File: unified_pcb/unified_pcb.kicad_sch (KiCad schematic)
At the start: 96 parts, among them J1 Conn_01x02_Socket, J2 USB_C_Receptacle, J3 Conn_01x02_Socket, J4 Conn_01x03_Pin, Q1 Q_Photo_NPN, Q2 Q_Photo_NPN, Q3 Q_Photo_NPN, SW1 SW_Push, SW2 SW_Push, U1 BQ27427YZFR, U10 3.3V LDO, U11 LMD4030T261-OA1, U12 LY4176D, U13 MMC5603NJ, U14 BMI270, U2 USBLC6-2P6, U3 3.3V LDO, U4 RP2350_60QFN, U7 QSPI Flash, U8 TPGLF72101CSP4, Y1 12MHz

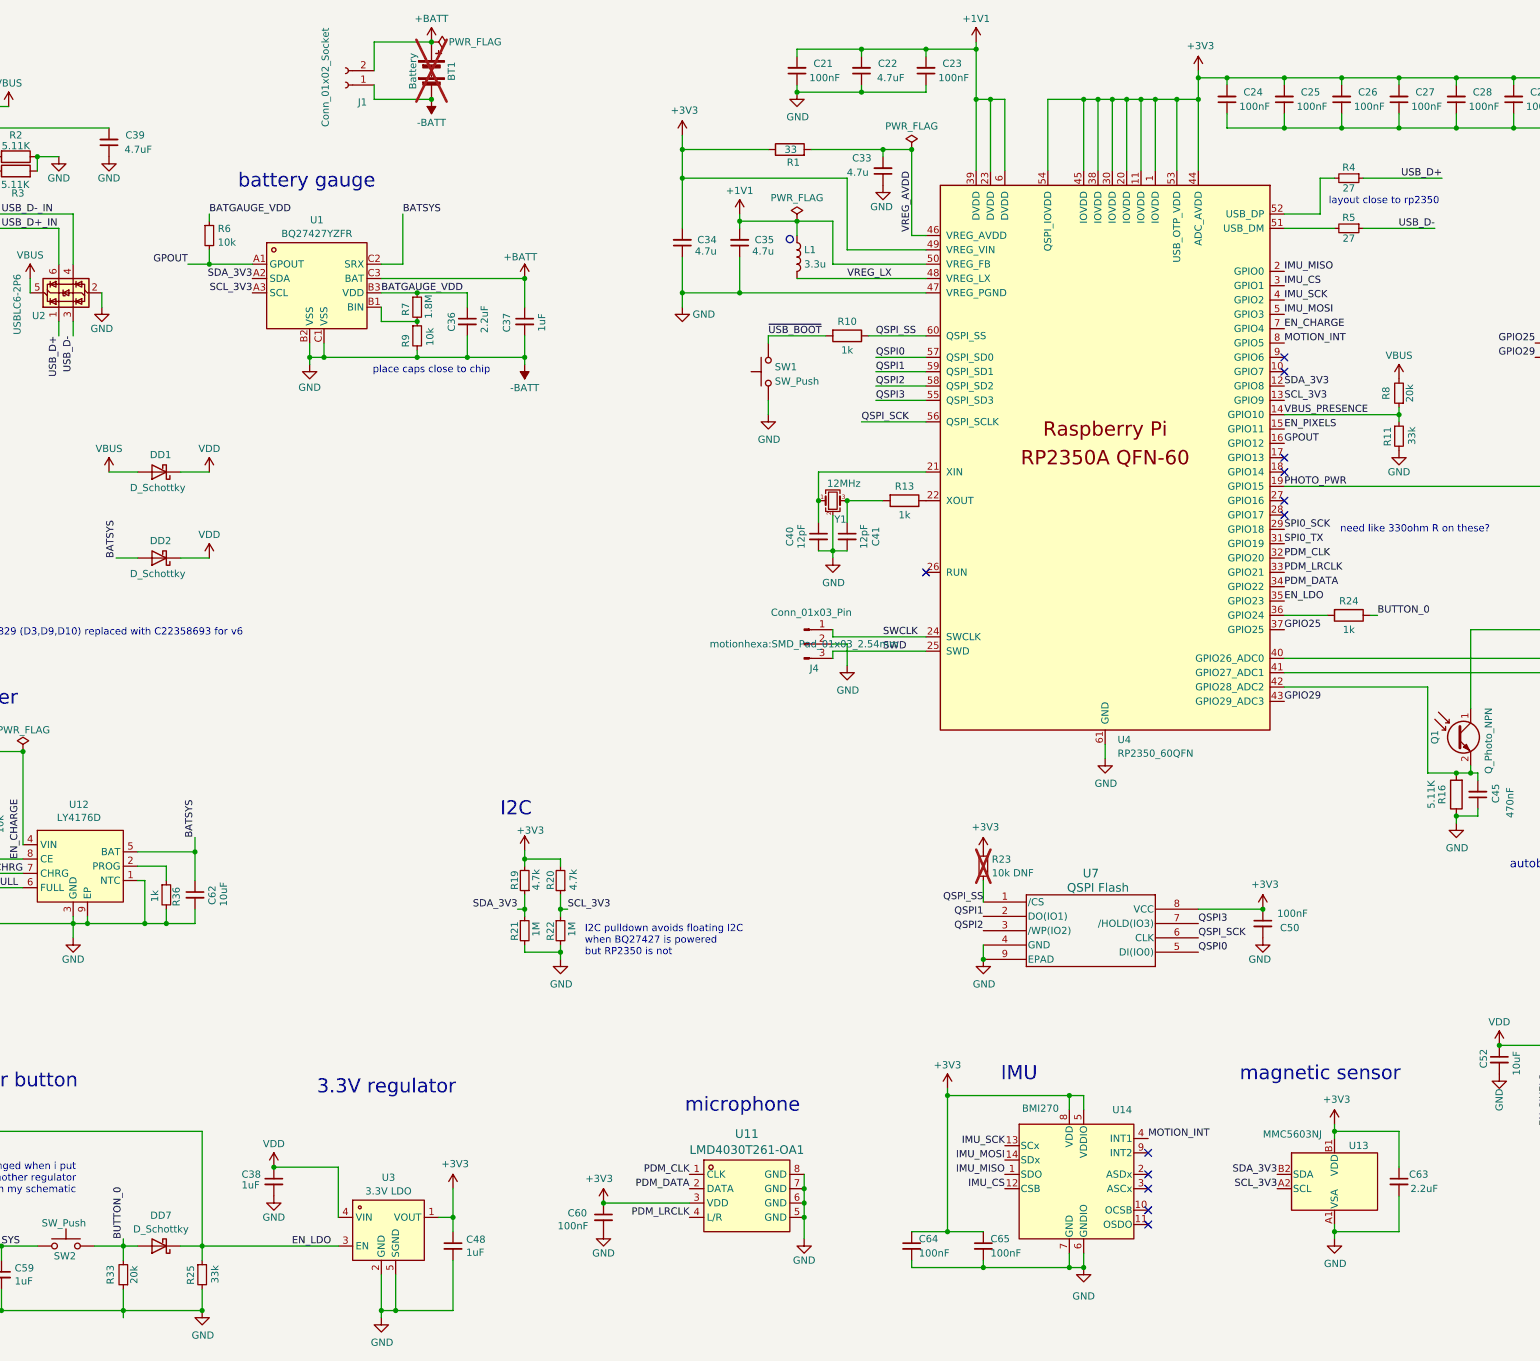
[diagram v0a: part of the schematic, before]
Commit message: ticking with dual ldo because moving to mosfets is unnecessary churn; lay out for magnetic sensor; layout cleanup
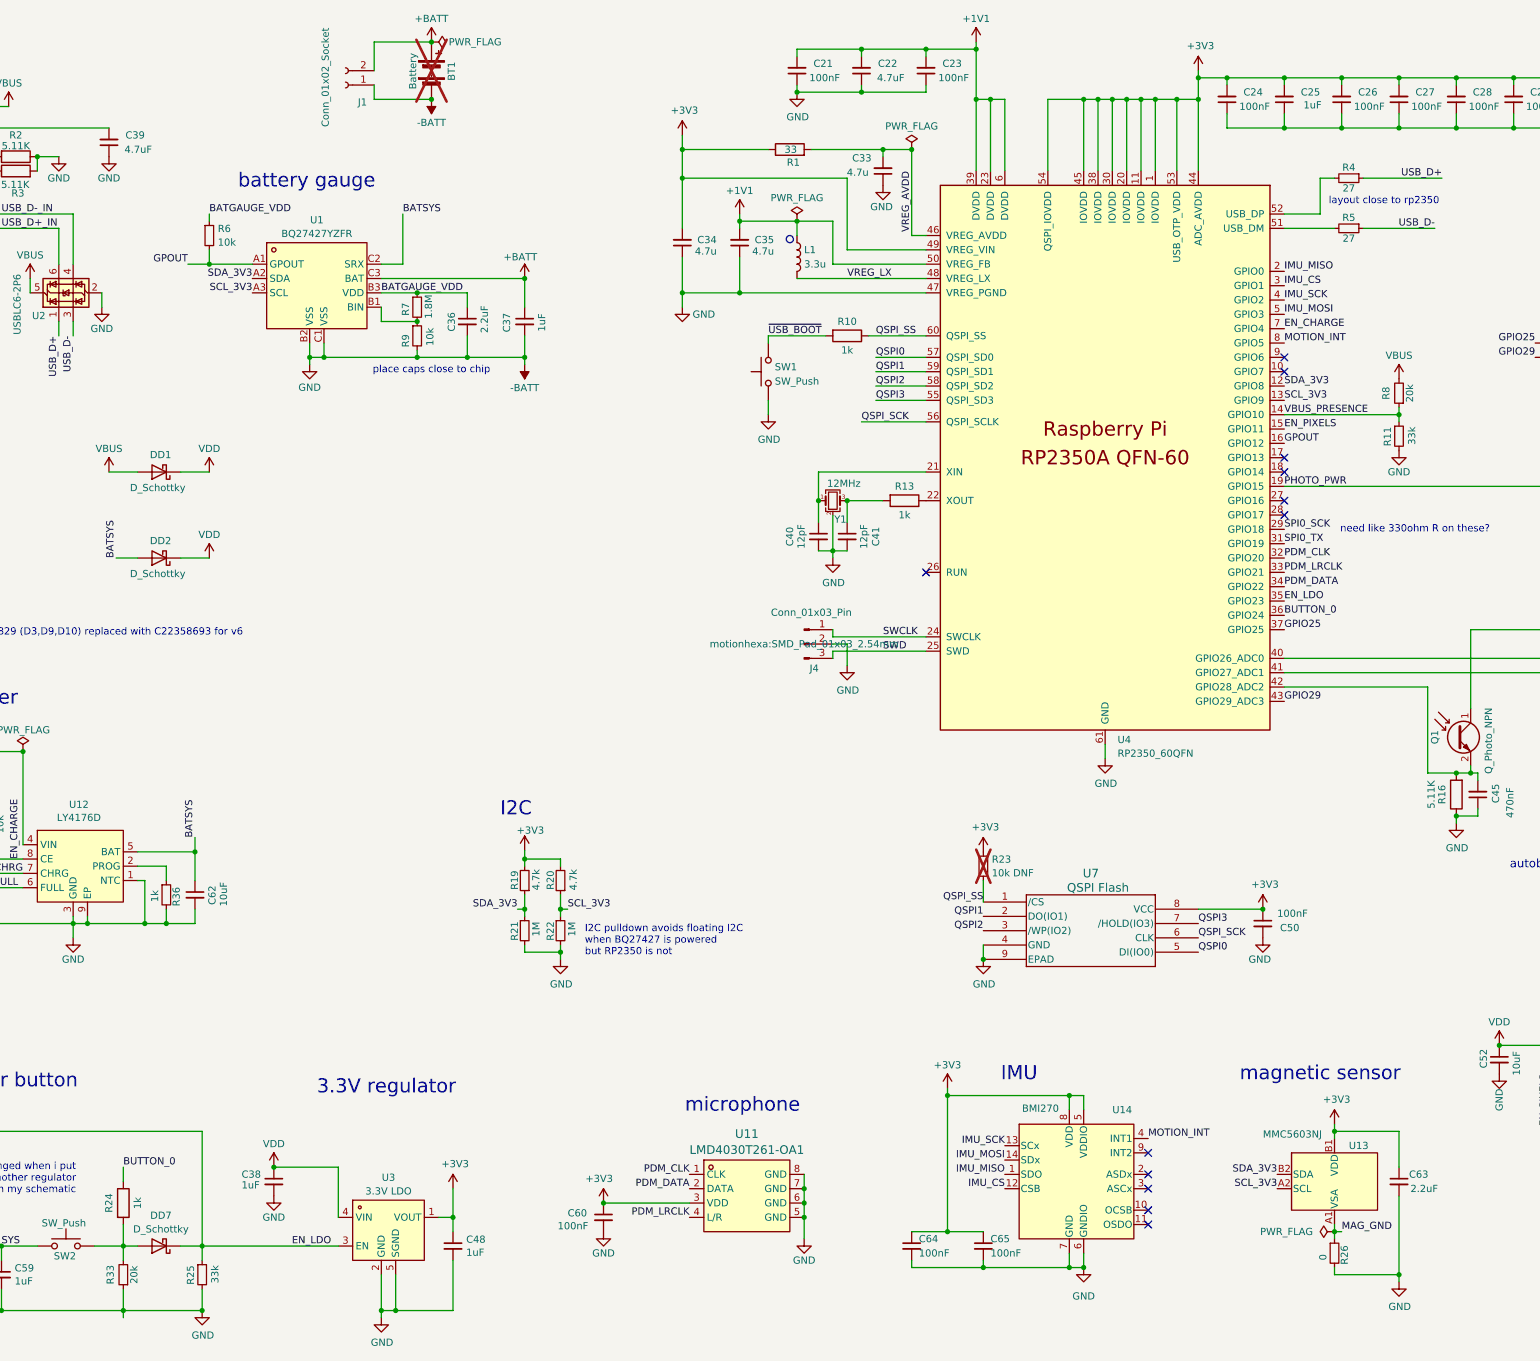
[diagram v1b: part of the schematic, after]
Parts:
- added R26: 0, Resistor_SMD:R_0402_1005Metric, symbol Device:R_Small
- C25: value 100nF -> 1uF; Designation CC0402KRX7R7BB104 -> CL05A105KP5NNNC; LCSC C60474 -> C14445
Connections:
- net -BATT: now also R26.2; no longer U13.A1 (VSA)
- net BUTTON_0: now also U4.36 (GPIO24); no longer DD7.2 (A), R33.2, SW2.2
- net at R24.2: now also DD7.2 (A), R33.2, SW2.2; no longer U4.36 (GPIO24)
- new net MAG_GND: R26.1, U13.A1 (VSA)
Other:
- moved on the sheet: R24

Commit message: u -> uF
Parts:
- C33, C34, C35: value 4.7u -> 4.7uF
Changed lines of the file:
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@@
 			)
 		)
-		(property "Value" "4.7u"
-			(at 183.896 65.024 0)
+		(property "Value" "4.7uF"
+			(at 184.658 65.278 0)
 			(effects
 				(font
@@
 			)
 		)
-		(property "Value" "4.7u"
-			(at 194.056 65.024 0)
+		(property "Value" "4.7uF"
+			(at 194.818 65.278 0)
 			(effects
 				(font
@@
 			)
 		)
-		(property "Value" "4.7u"
-			(at 210.82 51.054 0)
+		(property "Value" "4.7uF"
+			(at 210.566 50.8 0)
 			(effects
 				(font

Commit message: mag_gnd tweak; thermal vias
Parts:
- R16, R17, R18: Designation RC0402FR-07511KL -> RC0402FR-075K11L; LCSC C163461 -> C274895
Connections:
- net -BATT: no longer C63.2
- net MAG_GND: now also C63.2
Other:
- moved on the sheet: R26
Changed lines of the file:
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@@
 	)
 	(junction
+		(at 304.8 238.76)
+		(diameter 0)
+		(color 0 0 0 0)
+	)
+	(junction
 		(at 91.44 171.45)
 		(diameter 0)
@@
 	)
 	(junction
-		(at 304.8 246.38)
-		(diameter 0)
-		(color 0 0 0 0)
-	)
-	(junction
 		(at 340.36 157.48)
 		(diameter 0)
@@
 	(wire
 		(pts
-			(xy 293.37 246.38) (xy 293.37 245.11)
+			(xy 304.8 245.11) (xy 304.8 246.38)
 		)
 		(stroke
@@
 	(wire
 		(pts
-			(xy 304.8 232.41) (xy 304.8 246.38)
+			(xy 304.8 232.41) (xy 304.8 238.76)
 		)
 		(stroke
@@
 	(wire
 		(pts
-			(xy 294.64 238.76) (xy 293.37 238.76)
-		)
-		(stroke
-			(width 0)
-			(type default)
-		)
-	)
-	(wire
-		(pts
 			(xy 209.55 29.21) (xy 220.98 29.21)
 		)
@@
 	(wire
 		(pts
-			(xy 293.37 240.03) (xy 293.37 238.76)
+			(xy 304.8 240.03) (xy 304.8 238.76)
 		)
 		(stroke
@@
 	(wire
 		(pts
-			(xy 293.37 246.38) (xy 304.8 246.38)
-		)
-		(stroke
-			(width 0)
-			(type default)
-		)
-	)
-	(wire
-		(pts
 			(xy 246.38 242.57) (xy 246.38 245.11)
 		)
@@
 	(wire
 		(pts
-			(xy 304.8 247.65) (xy 304.8 246.38)
-		)
-		(stroke
-			(width 0)
-			(type default)
-		)
-	)
-	(wire
-		(pts
 			(xy 242.57 38.1) (xy 248.92 38.1)
 		)
@@
 	(wire
 		(pts
+			(xy 293.37 238.76) (xy 304.8 238.76)
+		)
+		(stroke
+			(width 0)
+			(type default)
+		)
+	)
+	(wire
+		(pts
 			(xy 156.21 172.72) (xy 156.21 173.99)
 		)
@@
 			)
 		)
-		(property "Designation" "RC0402FR-07511KL"
+		(property "Designation" "RC0402FR-075K11L"
 			(at 337.82 161.29 0)
 			(effects
@@
 			)
 		)
-		(property "LCSC" "C163461"
+		(property "LCSC" "C274895"
 			(at 337.82 161.29 90)
 			(effects
@@
 			)
 		)
-		(property "Designation" "RC0402FR-07511KL"
+		(property "Designation" "RC0402FR-075K11L"
 			(at 314.96 161.29 0)
 			(effects
@@
 			)
 		)
-		(property "LCSC" "C163461"
+		(property "LCSC" "C274895"
 			(at 314.96 161.29 90)
 			(effects
@@
 	(symbol
 		(lib_id "Device:R_Small")
-		(at 293.37 242.57 0)
+		(at 304.8 242.57 0)
 		(unit 1)
 		(exclude_from_sim no)
@@
 		(dnp no)
 		(property "Reference" "R26"
-			(at 295.148 244.602 90)
+			(at 306.578 244.602 90)
 			(effects
 				(font
@@
 		)
 		(property "Value" "0"
-			(at 291.338 243.84 90)
+			(at 302.768 243.84 90)
 			(effects
 				(font
@@
 		)
 		(property "Footprint" "Resistor_SMD:R_0402_1005Metric"
-			(at 293.37 242.57 0)
+			(at 304.8 242.57 0)
 			(effects
 				(font
@@
 		)
 		(property "Datasheet" "~"
-			(at 293.37 242.57 0)
+			(at 304.8 242.57 0)
 			(effects
 				(font
@@
 		)
 		(property "Description" "Resistor, small symbol"
-			(at 293.37 242.57 0)
+			(at 304.8 242.57 0)
 			(effects
 				(font
@@
 		)
 		(property "Designation" ""
-			(at 293.37 242.57 0)
+			(at 304.8 242.57 0)
 			(effects
 				(font
@@
 		)
 		(property "Field6" ""
-			(at 293.37 242.57 90)
+			(at 304.8 242.57 90)
 			(effects
 				(font
@@
 	(symbol
 		(lib_id "power:GND")
-		(at 304.8 247.65 0)
+		(at 304.8 246.38 0)
 		(unit 1)
 		(exclude_from_sim no)
@@
 		(dnp no)
 		(property "Reference" "#PWR033"
-			(at 304.8 254 0)
+			(at 304.8 252.73 0)
 			(effects
 				(font
@@
 		)
 		(property "Value" "GND"
-			(at 304.927 252.0442 0)
+			(at 304.927 250.7742 0)
 			(effects
 				(font
@@
 		)
 		(property "Footprint" ""
-			(at 304.8 247.65 0)
+			(at 304.8 246.38 0)
 			(effects
 				(font
@@
 		)
 		(property "Datasheet" ""
-			(at 304.8 247.65 0)
+			(at 304.8 246.38 0)
 			(effects
 				(font
@@
 		)
 		(property "Description" "Power symbol creates a global label with name \"GND\" , ground"
-			(at 304.8 247.65 0)
+			(at 304.8 246.38 0)
 			(effects
 				(font
@@
 			)
 		)
-		(property "Designation" "RC0402FR-07511KL"
+		(property "Designation" "RC0402FR-075K11L"
 			(at 358.14 161.29 0)
 			(effects
@@
 			)
 		)
-		(property "LCSC" "C163461"
+		(property "LCSC" "C274895"
 			(at 358.14 161.29 90)
 			(effects

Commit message: part nums and bom rationalization
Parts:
- C61: Designation (none) -> CL05A105KP5NNNC; LCSC (none) -> C14445
- C62: Designation (none) -> 0603X106K100; LCSC (none) -> C90806
- R14, R15, R19, R20, R32: Designation 0402WGF4701TCE -> FRC0402J472 TS; LCSC C25900 -> C2906941
- R26: Designation (none) -> 0402WGF0000TCE; LCSC (none) -> C17168
- R36: Designation (none) -> RC0402FR-071KL; LCSC (none) -> C106235
- U1: LCSC Part C6075475 -> (none)
- U10, U3: LCSC (none) -> C147954; LCSC Part C147954 -> (none)
- U13: MANUFACTURER Memsic -> (none)
- U14: MANUFACTURER Bosch Sensortec -> (none)
- U4: JLC C42411118 -> (none); LCSC (none) -> C42411118
- U8: symbol motionhexa:TPS22913BYZVR -> motionhexa:TPGLF72101CSP4
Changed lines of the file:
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@@
 			)
 		)
-		(property "Designation" "0402WGF4701TCE"
+		(property "Designation" "FRC0402J472 TS"
 			(at 45.72 172.72 0)
 			(effects
@@
 			)
 		)
-		(property "LCSC" "C25900"
+		(property "LCSC" "C2906941"
 			(at 45.72 172.72 90)
 			(effects
@@
 			)
 		)
-		(property "Designation" "0402WGF4701TCE"
+		(property "Designation" "FRC0402J472 TS"
 			(at 38.1 172.72 0)
 			(effects
@@
 			)
 		)
-		(property "LCSC" "C25900"
+		(property "LCSC" "C2906941"
 			(at 38.1 172.72 90)
 			(effects
@@
 	)
 	(symbol
-		(lib_id "motionhexa:TPS22913BYZVR")
+		(lib_id "motionhexa:TPGLF72101CSP4")
 		(at 345.44 208.28 0)
 		(unit 1)
@@
 		)
 		(property "Footprint" "motionhexa:YZV0004ADAD"
-			(at 345.44 208.28 0)
+			(at 344.932 216.662 0)
 			(effects
 				(font
@@
 		)
 		(property "Datasheet" "https://www.lcsc.com/datasheet/C42449029.pdf"
-			(at 345.44 208.28 0)
+			(at 345.186 219.202 0)
 			(effects
 				(font
@@
 			)
 		)
-		(property "LCSC Part" "C6075475"
-			(at 113.03 86.36 0)
-			(effects
-				(font
-					(size 1.27 1.27)
-				)
-				(hide yes)
-			)
-		)
 		(pin "A1"
 		)
@@
 			)
 		)
-		(property "MANUFACTURER" "Bosch Sensortec"
-			(at 247.65 229.87 0)
-			(effects
-				(font
-					(size 1.27 1.27)
-				)
-				(hide yes)
-			)
-		)
 		(property "LCSC" "C2836813"
 			(at 247.65 229.87 0)
@@
 			)
 		)
-		(property "Designation" "0402WGF4701TCE"
+		(property "Designation" "FRC0402J472 TS"
 			(at 156.21 176.53 0)
 			(effects
@@
 			)
 		)
-		(property "LCSC" "C25900"
+		(property "LCSC" "C2906941"
 			(at 156.21 176.53 90)
 			(effects
@@
 			)
 		)
-		(property "Designation" "0402WGF4701TCE"
+		(property "Designation" "FRC0402J472 TS"
 			(at 41.91 220.98 0)
 			(effects
@@
 			)
 		)
-		(property "LCSC" "C25900"
+		(property "LCSC" "C2906941"
 			(at 41.91 220.98 90)
 			(effects
@@
 			)
 		)
-		(property "Designation" "0402WGF4701TCE"
+		(property "Designation" "FRC0402J472 TS"
 			(at 149.86 176.53 0)
 			(effects
@@
 			)
 		)
-		(property "LCSC" "C25900"
+		(property "LCSC" "C2906941"
 			(at 149.86 176.53 90)
 			(effects
@@
 			)
 		)
+		(property "LCSC" "C14445"
+			(at 30.48 179.07 0)
+			(effects
+				(font
+					(size 1.27 1.27)
+				)
+				(hide yes)
+			)
+		)
+		(property "Designation" "CL05A105KP5NNNC"
+			(at 30.48 179.07 0)
+			(effects
+				(font
+					(size 1.27 1.27)
+				)
+				(hide yes)
+			)
+		)
 		(pin "1"
 		)
@@
 			)
 		)
+		(property "LCSC" "C90806"
+			(at 91.44 179.07 0)
+			(effects
+				(font
+					(size 1.27 1.27)
+				)
+				(hide yes)
+			)
+		)
+		(property "Designation" "0603X106K100"
+			(at 91.44 179.07 0)
+			(effects
+				(font
+					(size 1.27 1.27)
+				)
+				(hide yes)
+			)
+		)
 		(pin "1"
 		)
@@
 			)
 		)
+		(property "LCSC" "C106235"
+			(at 86.36 179.07 0)
+			(effects
+				(font
+					(size 1.27 1.27)
+				)
+				(hide yes)
+			)
+		)
+		(property "Designation" "RC0402FR-071KL"
+			(at 86.36 179.07 0)
+			(effects
+				(font
+					(size 1.27 1.27)
+				)
+				(hide yes)
+			)
+		)
 		(pin "1"
 		)
@@
 			)
 		)
-		(property "LCSC Part" "C147954"
-			(at 45.466 267.208 0)
+		(property "Designation" "RT9078-33GQZ"
+			(at 45.72 243.84 0)
 			(effects
 				(font
@@
 			)
 		)
-		(property "Designation" "RT9078-33GQZ"
+		(property "LCSC" "C147954"
 			(at 45.72 243.84 0)
 			(effects
@@
 			)
 		)
-		(property "Designation" ""
+		(property "LCSC" "C17168"
+			(at 304.8 242.57 0)
+			(effects
+				(font
+					(size 1.27 1.27)
+				)
+				(hide yes)
+			)
+		)
+		(property "Designation" "0402WGF0000TCE"
 			(at 304.8 242.57 0)
 			(effects
@@
 			)
 		)
-		(property "LCSC Part" "C147954"
-			(at 125.476 262.128 0)
+		(property "Designation" "RT9078-33GQZ"
+			(at 125.73 238.76 0)
 			(effects
 				(font
@@
 			)
 		)
-		(property "Designation" "RT9078-33GQZ"
+		(property "LCSC" "C147954"
 			(at 125.73 238.76 0)
 			(effects
@@
 			)
 		)
-		(property "JLC" "C42411118"
+		(property "LCSC" "C42411118"
 			(at 252.73 101.6 0)
 			(effects
@@
 			(at 293.37 229.87 0)
 			(effects
-				(font
-					(size 1.27 1.27)
-				)
-				(hide yes)
-			)
-		)
-		(property "MANUFACTURER" "Memsic"
-			(at 293.37 229.87 0)
-			(effects

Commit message: fix crystal part
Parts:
- C40, C41: value 12pF -> 15pF; Designation 0402N120F500CT -> 0402CG150J500NT; LCSC C555399 -> C1548
- Y1: footprint Crystal:Crystal_SMD_2520-4Pin_2.5x2.0mm -> Crystal:Crystal_SMD_3225-4Pin_3.2x2.5mm; Designation TXM12M0004252FBCEO00T -> ABM8-272-T3; LCSC C284155 -> C20625731
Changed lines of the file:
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@@
 			)
 		)
-		(property "Value" "12pF"
+		(property "Value" "15pF"
 			(at 209.9818 115.57 90)
 			(effects
@@
 			)
 		)
-		(property "Designation" "0402N120F500CT"
+		(property "Designation" "0402CG150J500NT"
 			(at 207.01 115.57 0)
 			(effects
@@
 			)
 		)
-		(property "LCSC" "C555399"
+		(property "LCSC" "C1548"
 			(at 207.01 115.57 90)
 			(effects
@@
 			)
 		)
-		(property "Footprint" "Crystal:Crystal_SMD_2520-4Pin_2.5x2.0mm"
+		(property "Footprint" "Crystal:Crystal_SMD_3225-4Pin_3.2x2.5mm"
 			(at 204.47 109.22 0)
 			(effects
@@
 			)
 		)
-		(property "Designation" "TXM12M0004252FBCEO00T"
+		(property "Designation" "ABM8-272-T3"
 			(at 204.47 109.22 0)
 			(effects
@@
 			)
 		)
-		(property "LCSC" "C284155"
+		(property "LCSC" "C20625731"
 			(at 204.47 109.22 90)
 			(effects
@@
 			)
 		)
-		(property "Value" "12pF"
+		(property "Value" "15pF"
 			(at 198.882 115.57 90)
 			(effects
@@
 			)
 		)
-		(property "Designation" "0402N120F500CT"
+		(property "Designation" "0402CG150J500NT"
 			(at 201.93 115.57 0)
 			(effects
@@
 			)
 		)
-		(property "LCSC" "C555399"
+		(property "LCSC" "C1548"
 			(at 201.93 115.57 90)
 			(effects
